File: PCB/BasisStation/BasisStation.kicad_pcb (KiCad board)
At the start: 2 copper layers, 160 x 135 mm, 21 parts, among them J1 Conn_02x05_Odd_Even, J2 Conn_02x03_Odd_Even, U2 ESP32-S3-WROOM-2

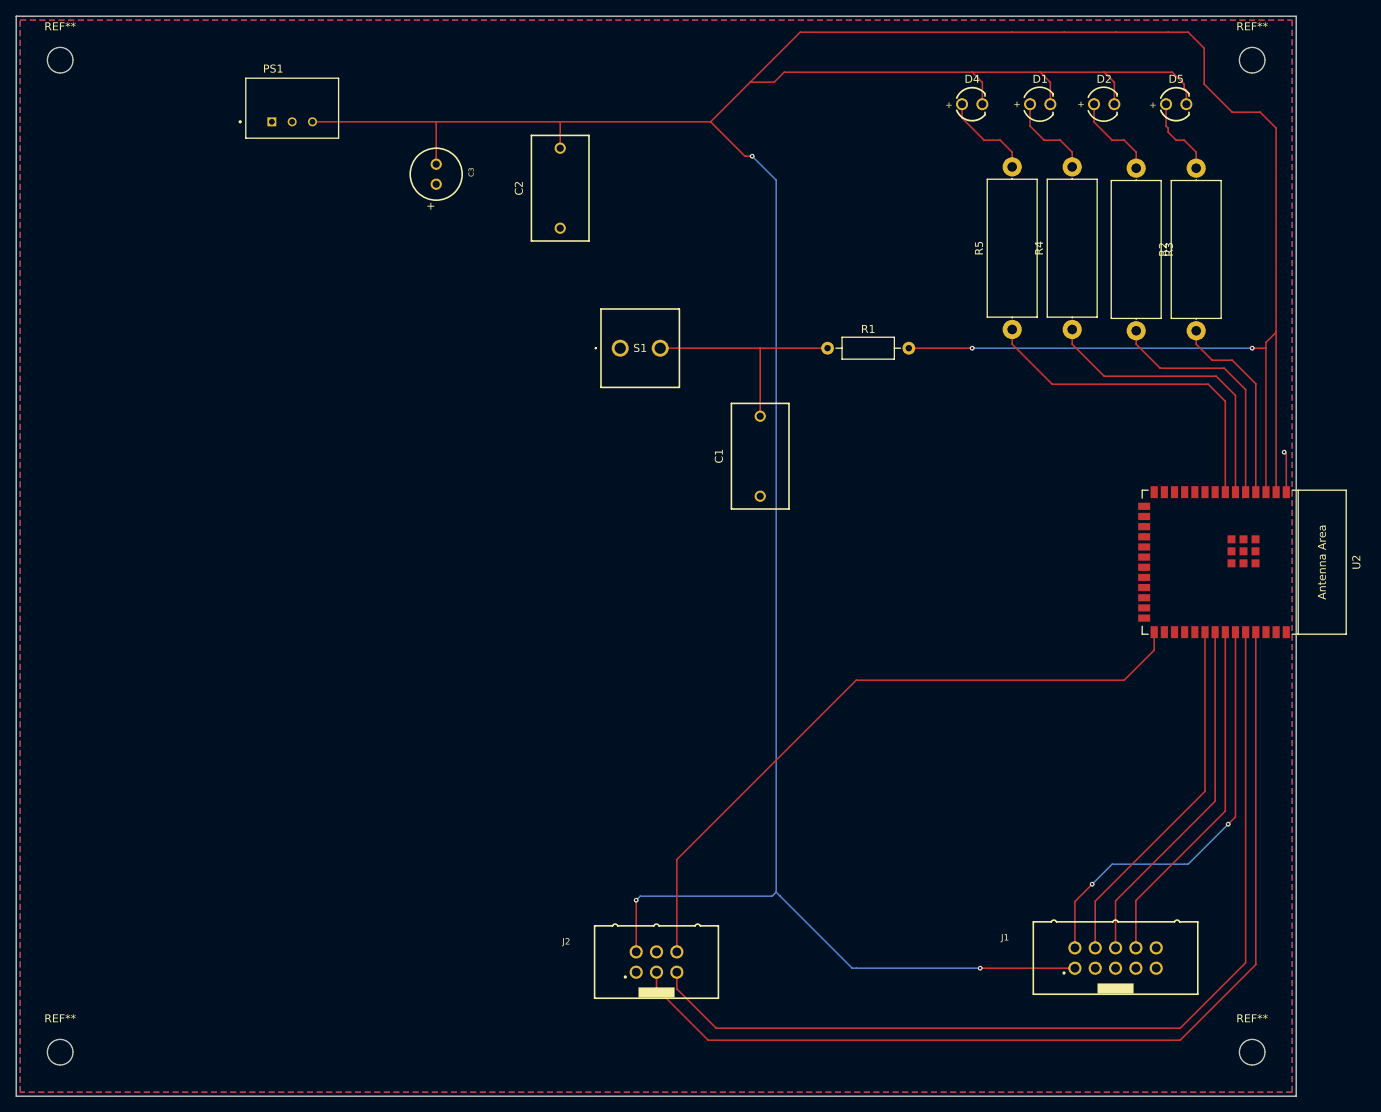
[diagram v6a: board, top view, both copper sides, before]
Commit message: microcontroller gewechselt und Layout angepasst
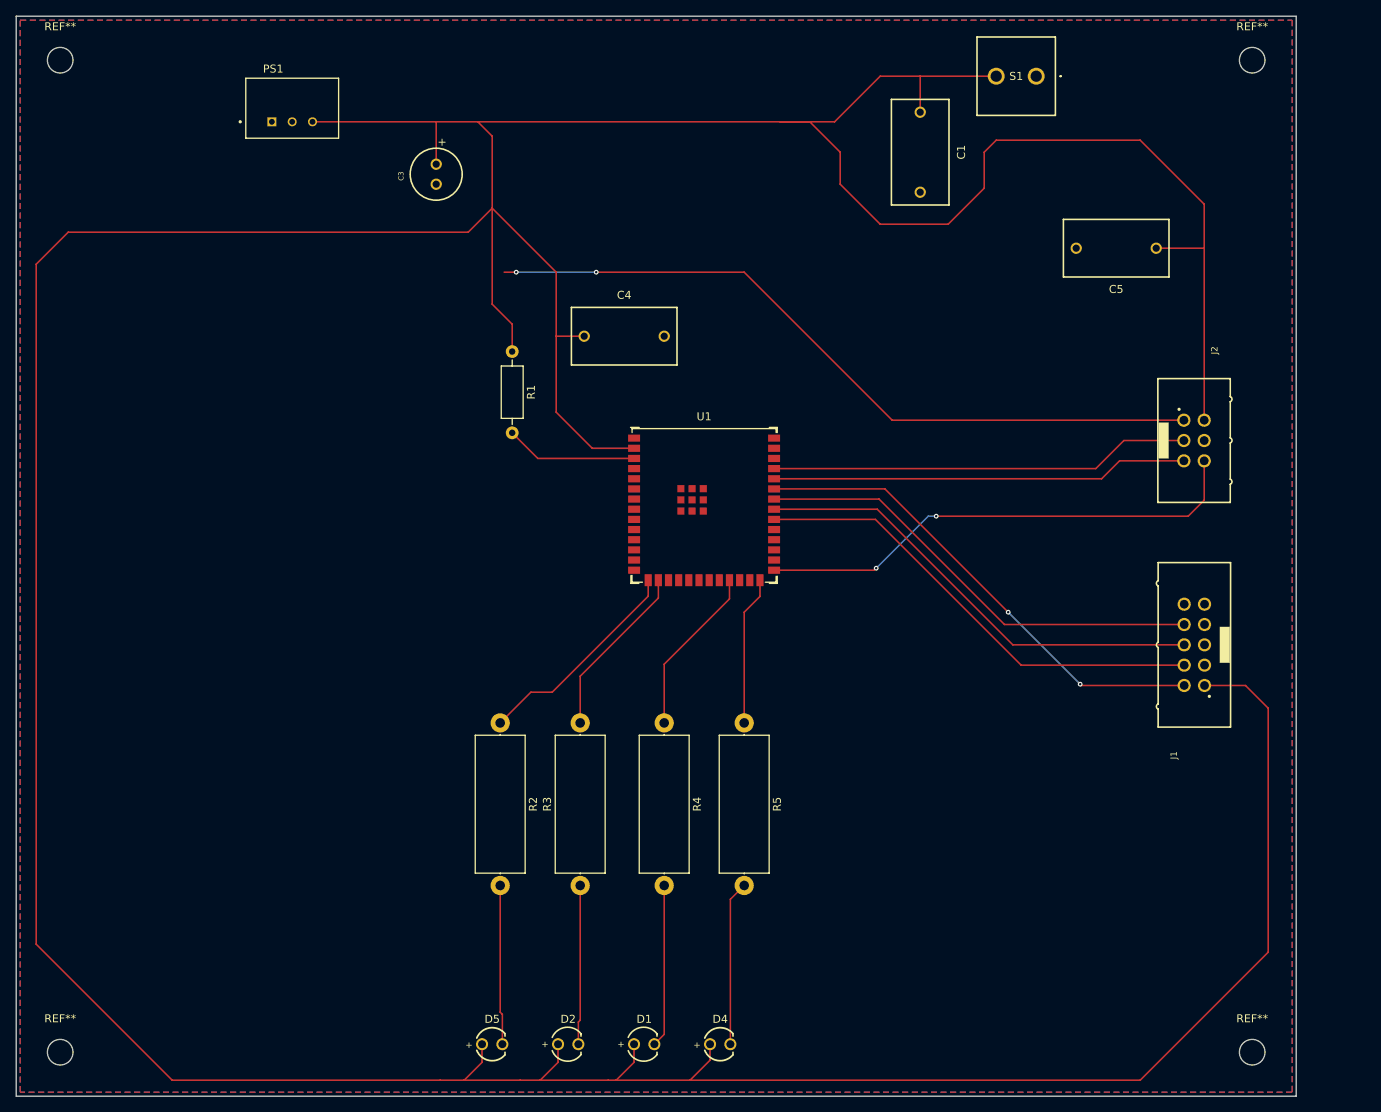
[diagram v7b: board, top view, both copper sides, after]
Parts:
- removed C2: WCAP-FTXX_P10, Footprints:WCAP-FTXX_P10L13W7H13
- removed U2: ESP32-S3-WROOM-2, Footprints:ESP32-S3-WROOM-2_NEW
- added C4: WCAP-FTXX_P10, Footprints:WCAP-FTXX_P10L13W7H13, F.Cu at (126.0, 65.0)
- added C5: WCAP-FTXX_P10, Footprints:WCAP-FTXX_P10L13W7H13, F.Cu at (187.5, 54.0)
- added U1: ESP32-S3-WROOM-1, Footprints:ESP32-S3-WROOM-1U, F.Cu at (136.0, 86.0)
- moved D5 145.3 mm to (109.5, 153.5)
- moved D2 135.3 mm to (119.0, 153.5)
- moved D1 127.5 mm to (128.5, 153.5)
- moved D4 121.6 mm to (138.0, 153.5)
- moved R3 113.4 mm to (120.5, 133.7), turned to 90 degrees
- moved R2 99.9 mm to (110.5, 113.3), turned to -90 degrees
- moved J2 93.6 mm to (197.2, 78.0), turned to -90 degrees
- moved R4 70.8 mm to (131.0, 113.3), turned to -90 degrees
- moved S1 62.1 mm to (177.5, 32.5), turned to 180 degrees
- moved R5 59.5 mm to (141.0, 113.3), turned to -90 degrees
- moved C1 42.9 mm to (163.0, 42.0), turned to -90 degrees
- moved J1 40.4 mm to (197.3, 103.6), turned to 90 degrees
- moved R1 39.4 mm to (112.0, 66.9), turned to -90 degrees
- turned C3 to 90 degrees
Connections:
- C1 pad 1: GND -> +3V3
- C1 pad 2: Net-(C1-Pad2) -> GND
- C3 pad 1: GND -> +3V3
- C3 pad 2: +3V3 -> GND
- D1 pad 1: +3V3 -> Net-(D1-K)
- D1 pad 2: Net-(D1-A) -> +3V3
- D2 pad 1: +3V3 -> Net-(D2-K)
- D2 pad 2: Net-(D2-A) -> +3V3
- D4 pad 1: Net-(D4-A) -> +3V3
- D4 pad 2: +3V3 -> Net-(D4-K)
- D5 pad 1: Net-(D5-Pad1) -> +3V3
- D5 pad 2: +3V3 -> Net-(D5-Pad2)
- J2 pad 1: /EN -> EN
- J2 pad 3: TXD0 -> Net-(J2-Pin_3)
- J2 pad 5: RXD0 -> Net-(J2-Pin_5)
- J2 pad 6: IO0 -> Net-(J2-Pin_6)
- R1 pad 1: Net-(C1-Pad2) -> +3V3
- R1 pad 2: Net-(PS1-+VOUT) -> EN
- R2 pad 2: Net-(D5-Pad1) -> Net-(D5-Pad2)
- R3 pad 1: Net-(D2-A) -> Net-(D2-K)
- R4 pad 2: Net-(D1-A) -> Net-(D1-K)
- R5 pad 2: Net-(D4-A) -> Net-(D4-K)
- S1 pad 2: Net-(C1-Pad2) -> +3V3
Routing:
- net +3V3: track 489.4 -> 650.0 mm, vias 5 -> 0
- net TXD0: track 125.1 -> 0.00 mm
- net RXD0: track 119.9 -> 0.00 mm
- net EN: track 0.00 -> 109.2 mm, vias 0 -> 2
- net IO0: track 84.3 -> 0.00 mm
- net Net-(J2-Pin_6): track 0.00 -> 62.3 mm, vias 0 -> 2
- net Net-(J2-Pin_3): track 0.00 -> 52.7 mm
- net Net-(J2-Pin_5): track 0.00 -> 52.2 mm
- net Net-(C1-Pad2): track 29.4 -> 0.00 mm
- net Net-(U1-GPIO45): track 42.8 -> 18.7 mm
- net Net-(D4-K): track 0.00 -> 20.6 mm
- net Net-(D1-K): track 0.00 -> 20.3 mm
- net Net-(D5-Pad2): track 0.00 -> 20.0 mm
- net Net-(D2-K): track 0.00 -> 19.9 mm
- net Net-(U1-GPIO21): track 37.0 -> 21.2 mm
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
